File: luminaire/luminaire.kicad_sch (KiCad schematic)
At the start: 23 parts, among them Q1 FMMT618, SW1 SW_DP3T, U1 zxsc310

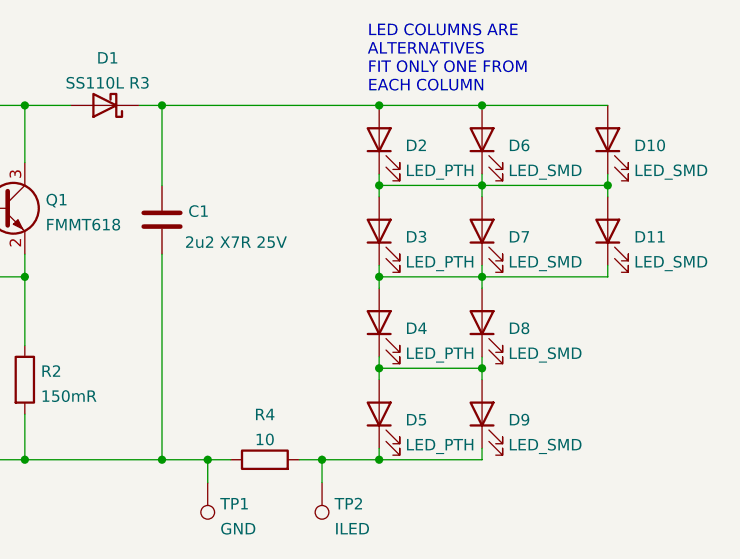
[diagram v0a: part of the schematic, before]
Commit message: Remove PTH LEDs
They are kinda massive, make layout awkward, and have really narrow
viewing angles.
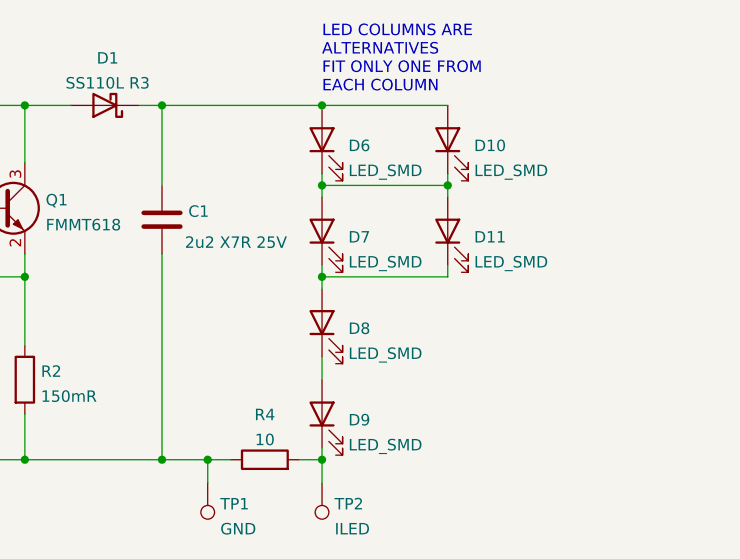
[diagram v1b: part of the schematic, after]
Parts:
- removed D2, D3, D4, D5: LED_PTH, LED_THT:LED_D5.0mm_Clear, symbol Device:LED
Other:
- moved on the sheet: D10, D11, D6, D7, D8, D9

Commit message: Finalise design
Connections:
- net at BT1.2 (-), C1.2, R2.2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: no longer U1.3 (STDN)
- net at L1.1, SW1.2, SW1.4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: now also U1.3 (STDN)
- net at D6.1 (K), D7.2 (A): no longer D10.1 (K), D11.2 (A)
- new net: D10.1 (K), D11.2 (A)
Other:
- note added: "LED COLUMNS ARE ALTERNATIVES FIT ONLY ONE COLUMN"
- note removed: "LED COLUMNS ARE ALTERNATIVES FIT ONLY ONE FROM EACH COLUMN"
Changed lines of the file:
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@@
   (junction (at 92.71 67.31) (diameter 0) (color 0 0 0 0)
   )
-  (junction (at 220.98 76.2) (diameter 0) (color 0 0 0 0)
-  )
   (junction (at 160.02 86.36) (diameter 0) (color 0 0 0 0)
   )
-  (junction (at 207.01 76.2) (diameter 0) (color 0 0 0 0)
+  (junction (at 95.25 67.31) (diameter 0) (color 0 0 0 0)
   )
   (junction (at 173.99 106.68) (diameter 0) (color 0 0 0 0)
@@
   (junction (at 160.02 106.68) (diameter 0) (color 0 0 0 0)
   )
-  (junction (at 104.14 106.68) (diameter 0) (color 0 0 0 0)
+  (junction (at 96.52 106.68) (diameter 0) (color 0 0 0 0)
+  )
+  (junction (at 96.52 78.74) (diameter 0) (color 0 0 0 0)
   )
   (junction (at 207.01 86.36) (diameter 0) (color 0 0 0 0)
@@
     (stroke (width 0) (type default) (color 0 0 0 0))
   )
-  (wire (pts (xy 207.01 76.2) (xy 207.01 77.47))
-    (stroke (width 0) (type default) (color 0 0 0 0))
-  )
   (wire (pts (xy 90.17 69.85) (xy 92.71 69.85))
     (stroke (width 0) (type default) (color 0 0 0 0))
@@
     (stroke (width 0) (type default) (color 0 0 0 0))
   )
+  (wire (pts (xy 96.52 106.68) (xy 101.6 106.68))
+    (stroke (width 0) (type default) (color 0 0 0 0))
+  )
   (wire (pts (xy 173.99 67.31) (xy 173.99 73.66))
     (stroke (width 0) (type default) (color 0 0 0 0))
@@
     (stroke (width 0) (type default) (color 0 0 0 0))
   )
-  (wire (pts (xy 207.01 76.2) (xy 220.98 76.2))
-    (stroke (width 0) (type default) (color 0 0 0 0))
-  )
   (wire (pts (xy 129.54 83.82) (xy 133.35 83.82))
     (stroke (width 0) (type default) (color 0 0 0 0))
@@
     (stroke (width 0) (type default) (color 0 0 0 0))
   )
+  (wire (pts (xy 104.14 83.82) (xy 96.52 83.82))
+    (stroke (width 0) (type default) (color 0 0 0 0))
+  )
   (wire (pts (xy 207.01 85.09) (xy 207.01 86.36))
     (stroke (width 0) (type default) (color 0 0 0 0))
@@
     (stroke (width 0) (type default) (color 0 0 0 0))
   )
-  (wire (pts (xy 104.14 106.68) (xy 160.02 106.68))
+  (wire (pts (xy 95.25 63.5) (xy 95.25 67.31))
     (stroke (width 0) (type default) (color 0 0 0 0))
   )
@@
     (stroke (width 0) (type default) (color 0 0 0 0))
   )
-  (wire (pts (xy 104.14 83.82) (xy 104.14 106.68))
-    (stroke (width 0) (type default) (color 0 0 0 0))
-  )
-  (wire (pts (xy 101.6 106.68) (xy 104.14 106.68))
+  (wire (pts (xy 101.6 106.68) (xy 160.02 106.68))
     (stroke (width 0) (type default) (color 0 0 0 0))
   )
@@
     (stroke (width 0) (type default) (color 0 0 0 0))
   )
-  (wire (pts (xy 71.12 106.68) (xy 101.6 106.68))
+  (wire (pts (xy 71.12 106.68) (xy 96.52 106.68))
     (stroke (width 0) (type default) (color 0 0 0 0))
   )
@@
     (stroke (width 0) (type default) (color 0 0 0 0))
   )
+  (wire (pts (xy 96.52 83.82) (xy 96.52 78.74))
+    (stroke (width 0) (type default) (color 0 0 0 0))
+  )
   (wire (pts (xy 153.67 86.36) (xy 160.02 86.36))
     (stroke (width 0) (type default) (color 0 0 0 0))
@@
     (stroke (width 0) (type default) (color 0 0 0 0))
   )
-  (wire (pts (xy 220.98 76.2) (xy 220.98 77.47))
-    (stroke (width 0) (type default) (color 0 0 0 0))
-  )
-  (wire (pts (xy 220.98 74.93) (xy 220.98 76.2))
+  (wire (pts (xy 220.98 74.93) (xy 220.98 77.47))
+    (stroke (width 0) (type default) (color 0 0 0 0))
+  )
+  (wire (pts (xy 96.52 106.68) (xy 96.52 110.49))
     (stroke (width 0) (type default) (color 0 0 0 0))
   )
@@
     (stroke (width 0) (type default) (color 0 0 0 0))
   )
-  (wire (pts (xy 92.71 67.31) (xy 96.52 67.31))
+  (wire (pts (xy 92.71 67.31) (xy 95.25 67.31))
     (stroke (width 0) (type default) (color 0 0 0 0))
   )
@@
     (stroke (width 0) (type default) (color 0 0 0 0))
   )
-  (wire (pts (xy 207.01 74.93) (xy 207.01 76.2))
+  (wire (pts (xy 95.25 67.31) (xy 96.52 67.31))
+    (stroke (width 0) (type default) (color 0 0 0 0))
+  )
+  (wire (pts (xy 207.01 74.93) (xy 207.01 77.47))
     (stroke (width 0) (type default) (color 0 0 0 0))
   )
@@
     (stroke (width 0) (type default) (color 0 0 0 0))
   )
-  (text "LED COLUMNS ARE\nALTERNATIVES\nFIT ONLY ONE FROM\nEACH COLUMN"
-    (at 207.01 66.04 0)
+  (text "LED COLUMNS ARE\nALTERNATIVES\nFIT ONLY ONE COLUMN" (at 207.01 66.04 0)
     (effects (font (size 1.27 1.27)) (justify left bottom))
   )
@@
     (pin "1")
     (pin "2")
+  )
+  (symbol (lib_id "power:PWR_FLAG") (at 95.25 63.5 0) (unit 1)
+    (in_bom yes) (on_board yes) (fields_autoplaced)
+    (property "Reference" "#FLG0101" (id 0) (at 95.25 61.595 0)
+      (effects (font (size 1.27 1.27)) hide)
+    )
+    (property "Value" "PWR_FLAG" (id 1) (at 95.25 59.8955 0))
+    (property "Footprint" "" (id 2) (at 95.25 63.5 0)
+      (effects (font (size 1.27 1.27)) hide)
+    )
+    (property "Datasheet" "~" (id 3) (at 95.25 63.5 0)
+      (effects (font (size 1.27 1.27)) hide)
+    )
+    (pin "1")
   )
   (symbol (lib_id "Device:L") (at 129.54 67.31 90) (unit 1)
@@
     (pin "2")
   )
+  (symbol (lib_id "power:PWR_FLAG") (at 96.52 110.49 180) (unit 1)
+    (in_bom yes) (on_board yes) (fields_autoplaced)
+    (property "Reference" "#FLG0102" (id 0) (at 96.52 112.395 0)
+      (effects (font (size 1.27 1.27)) hide)
+    )
+    (property "Value" "PWR_FLAG" (id 1) (at 98.171 112.239 0)
+      (effects (font (size 1.27 1.27)) (justify right))
+    )
+    (property "Footprint" "" (id 2) (at 96.52 110.49 0)
+      (effects (font (size 1.27 1.27)) hide)
+    )
+    (property "Datasheet" "~" (id 3) (at 96.52 110.49 0)
+      (effects (font (size 1.27 1.27)) hide)
+    )
+    (pin "1")
+  )
   (symbol (lib_id "Device:D_Schottky") (at 182.88 67.31 180) (unit 1)
     (in_bom yes) (on_board yes) (fields_autoplaced)
@@
   )
   (symbol_instances
+    (path "/5897adf1-aa08-4983-98b1-5410bc04e66d"
+      (reference "#FLG0101") (unit 1) (value "PWR_FLAG") (footprint "")
+    )
+    (path "/a3681e58-b281-4585-bcfb-3b4d0ccf52e1"
+      (reference "#FLG0102") (unit 1) (value "PWR_FLAG") (footprint "")
+    )
     (path "/01c49248-5188-438f-8b42-9b6da61b9284"
       (reference "BT1") (unit 1) (value "1xAA Holder") (footprint "Battery:BatteryHolder_Keystone_2460_1xAA")

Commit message: Finalise BOM and gerbers
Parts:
- SW1: Farnell (none) -> 2978768
- SW1: Farnell 2854760 -> 2978768
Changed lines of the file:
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@@
+      (effects (font (size 1.27 1.27)) hide)
+    )
+    (property "Farnell" "2978768" (id 4) (at 143.51 93.98 0)
       (effects (font (size 1.27 1.27)) hide)
     )
@@
       (effects (font (size 1.27 1.27)) hide)
     )
-    (property "Farnell" "2854760" (id 4) (at 85.09 67.31 0)
+    (property "Farnell" "2978768" (id 4) (at 85.09 67.31 0)
       (effects (font (size 1.27 1.27)) hide)
     )

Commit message: Annotate schematic with measured currents
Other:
- note added: "MEASURED I_LO = 5.6mA I_HI = 10.7mA"
- note added: "MEASURED I_LO = 51mA I_HI = 95mA Cell voltage 1.4V Est life: 26-49 hrs"
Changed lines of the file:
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@@
     (stroke (width 0) (type default) (color 0 0 0 0))
+  )
+  (text "MEASURED\nI_LO = 5.6mA\nI_HI = 10.7mA" (at 195.58 123.19 0)
+    (effects (font (size 1.27 1.27)) (justify left bottom))
+  )
+  (text "MEASURED\nI_LO = 51mA\nI_HI = 95mA\nCell voltage 1.4V\nEst life: 26-49 hrs"
+    (at 50.8 81.28 0)
+    (effects (font (size 1.27 1.27)) (justify left bottom))
   )
   (text "LED COLUMNS ARE\nALTERNATIVES\nFIT ONLY ONE COLUMN" (at 207.01 66.04 0)
